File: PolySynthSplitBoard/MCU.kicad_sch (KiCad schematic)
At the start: 88 parts, among them J401 PWR, J402 DATA, J403 SWD Header, J404 MIDI_In, J405 Micro_SD_Card_Det2, J406 MIDI_Out, J407 MIDI_Thru, SW401 RST, SW402 BOOT, U401 STM32F411RETx, U404 74HC04, U405 6N138, Y401 16MHz, Y402 32.768kHZ

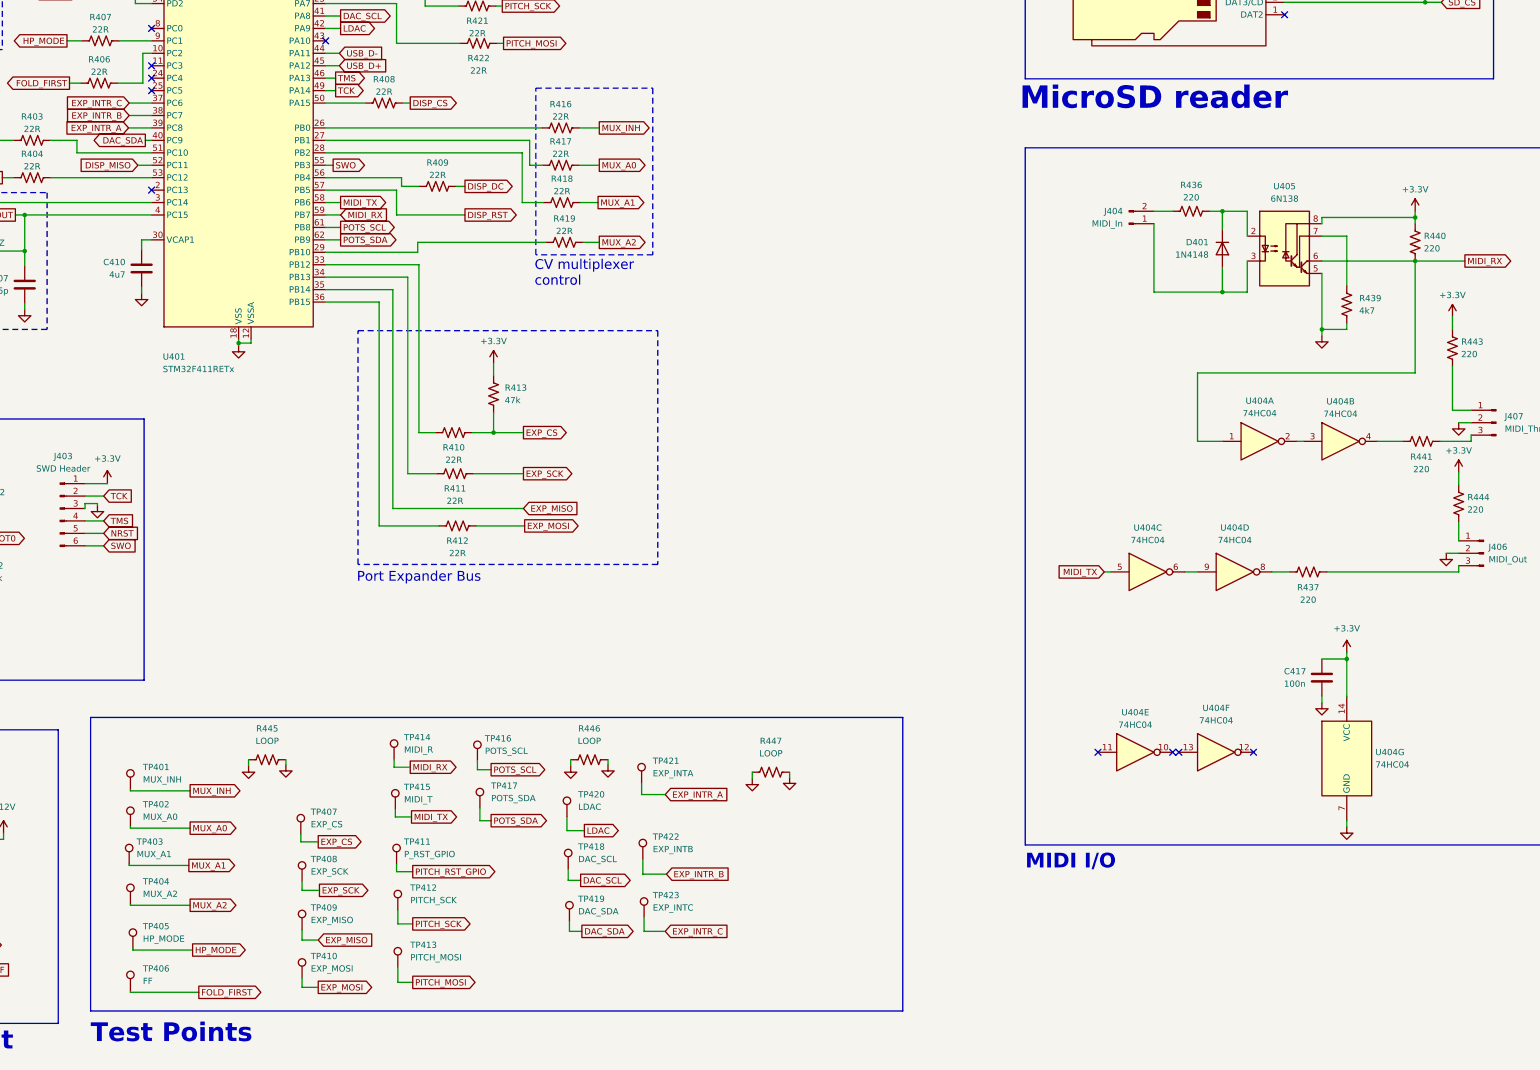
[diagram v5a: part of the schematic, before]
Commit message: double buffering voice clock fixes
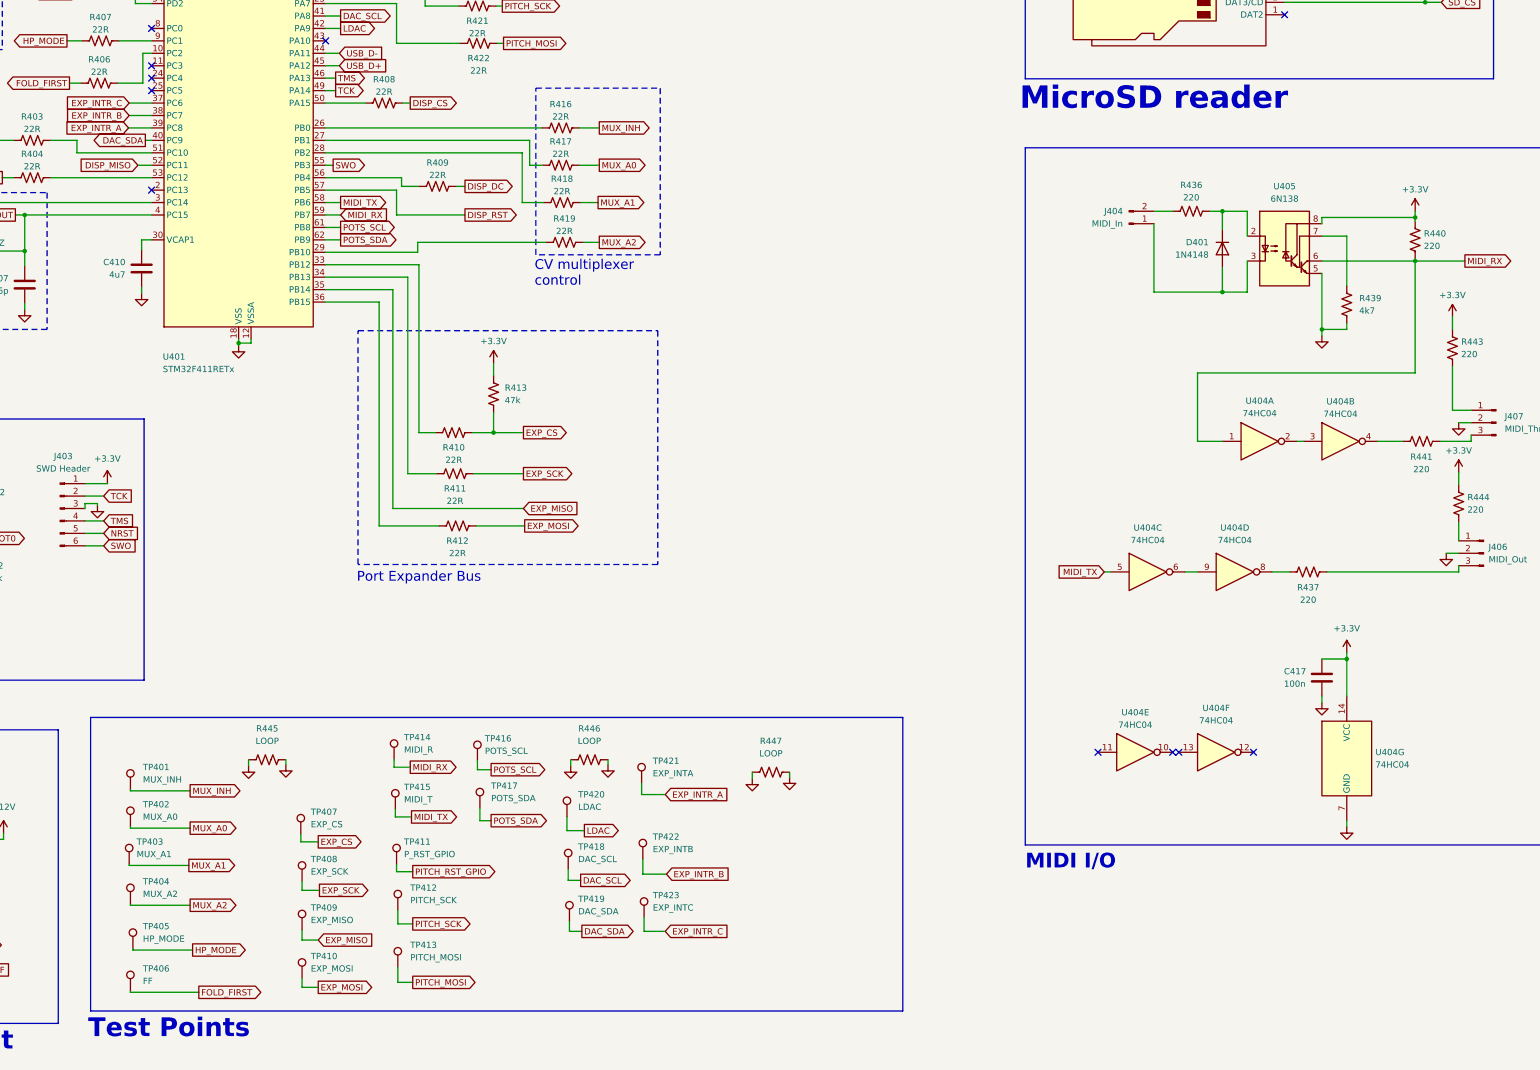
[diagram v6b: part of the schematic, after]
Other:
- moved on the sheet: R440
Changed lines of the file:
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@@
 	(wire
 		(pts
-			(xy 343.662 108.966) (xy 343.662 110.236)
+			(xy 343.662 108.966) (xy 343.662 109.728)
 		)
 		(stroke
@@
 	(wire
 		(pts
+			(xy 343.662 117.348) (xy 343.662 117.856)
+		)
+		(stroke
+			(width 0)
+			(type default)
+		)
+	)
+	(wire
+		(pts
 			(xy 152.146 221.742) (xy 154.94 221.742)
 		)
@@
 	(rectangle
 		(start 164.084 82.55)
-		(end 187.96 116.586)
+		(end 189.484 116.586)
 		(stroke
 			(width 0)
@@
 	(text "Test Points"
 		(exclude_from_sim no)
-		(at 73.152 277.876 0)
+		(at 72.644 276.86 0)
 		(effects
 			(font
@@
 	(symbol
 		(lib_id "Device:R_US")
-		(at 343.662 114.046 0)
+		(at 343.662 113.538 0)
 		(unit 1)
 		(exclude_from_sim no)
@@
 		(fields_autoplaced yes)
 		(property "Reference" "R440"
-			(at 345.44 112.776 0)
+			(at 345.44 112.268 0)
 			(effects
 				(font
@@
 		)
 		(property "Value" "220"
-			(at 345.44 115.316 0)
+			(at 345.44 114.808 0)
 			(effects
 				(font
@@
 		)
 		(property "Footprint" "Resistor_SMD:R_0805_2012Metric"
-			(at 344.678 114.3 90)
+			(at 344.678 113.792 90)
 			(effects
 				(font
@@
 		)
 		(property "Datasheet" "~"
-			(at 343.662 114.046 0)
+			(at 343.662 113.538 0)
 			(effects
 				(font
@@
 		)
 		(property "Description" ""
-			(at 343.662 114.046 0)
+			(at 343.662 113.538 0)
 			(effects
 				(font
